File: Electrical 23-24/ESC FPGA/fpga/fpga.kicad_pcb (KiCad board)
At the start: 2 copper layers, 85 x 56 mm, 174 parts, among them J1 SBH11-PBPC-D07-ST-BK, J2 LSHM-110-04.0-L-DV-A-N-K-TR, J3 USB_B_Micro, J4 LSHM-110-04.0-L-DV-A-N-K-TR, J5 Conn_02x06_Top_Bottom, J6 Conn_02x06_Top_Bottom, J7 Conn_02x20_Odd_Even, J8 Conn_02x06_Top_Bottom, J9 Conn_01x01_Pin, SW1 SW_SPDT, SW10 SW_SPDT, SW11 SW_SPDT, SW2 SW_Push, SW3 SW_SPDT, SW4 SW_SPDT, SW5 SW_SPDT, SW6 SW_Push, SW7 SW_Push, SW8 SW_Push, SW9 SW_SPDT, U1 XC6SLX9-TQG144, U12 MIC28515T-E/PHA, U13 FXMA108BQX, U14 FXMA108BQX, U15 FXMA108BQX, U5 MT25QL128ABA1ESE, U6 MIC28515T-E/PHA, U7 MIC28515T-E/PHA, U8 LM74700QDBVRQ1, U9 LM74700QDBVRQ1, X1 KC5032Z100.000C1JX00

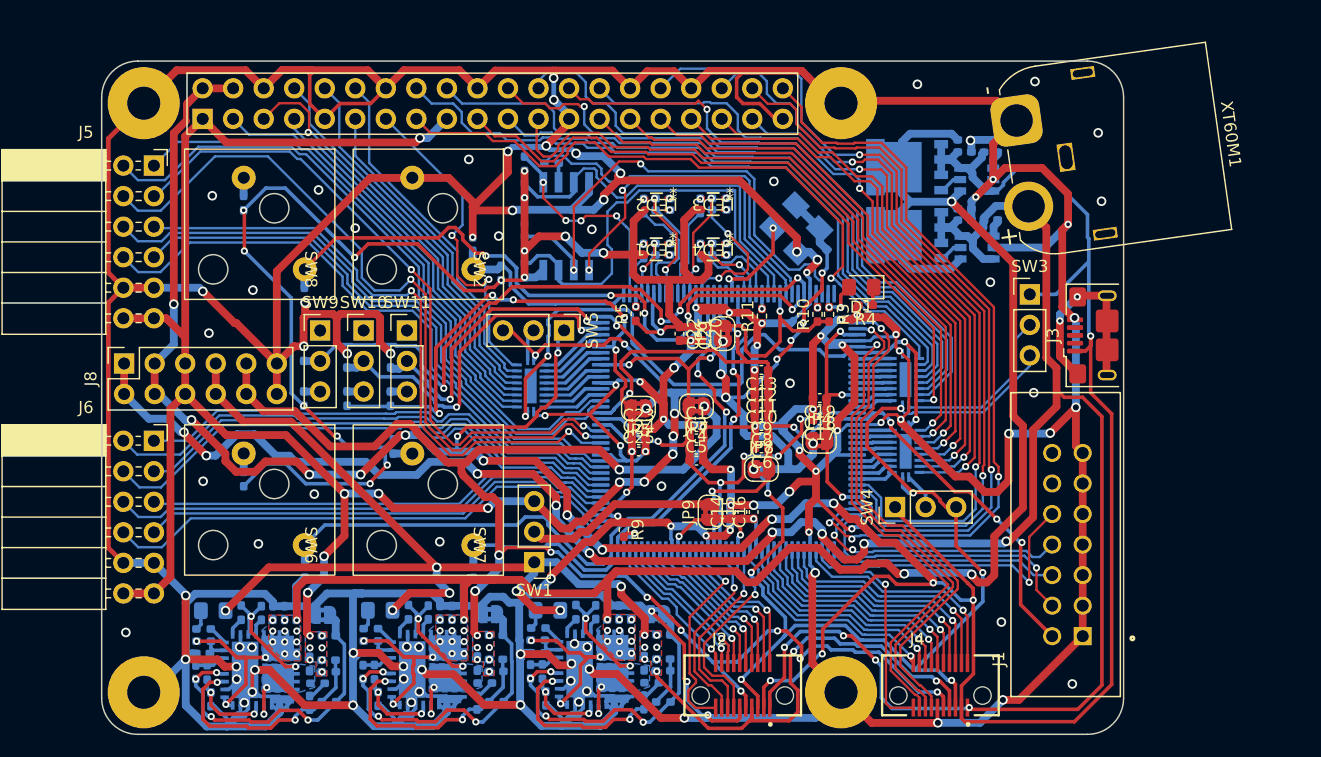
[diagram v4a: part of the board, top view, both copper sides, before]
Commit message: Add silkscreen to FPGA
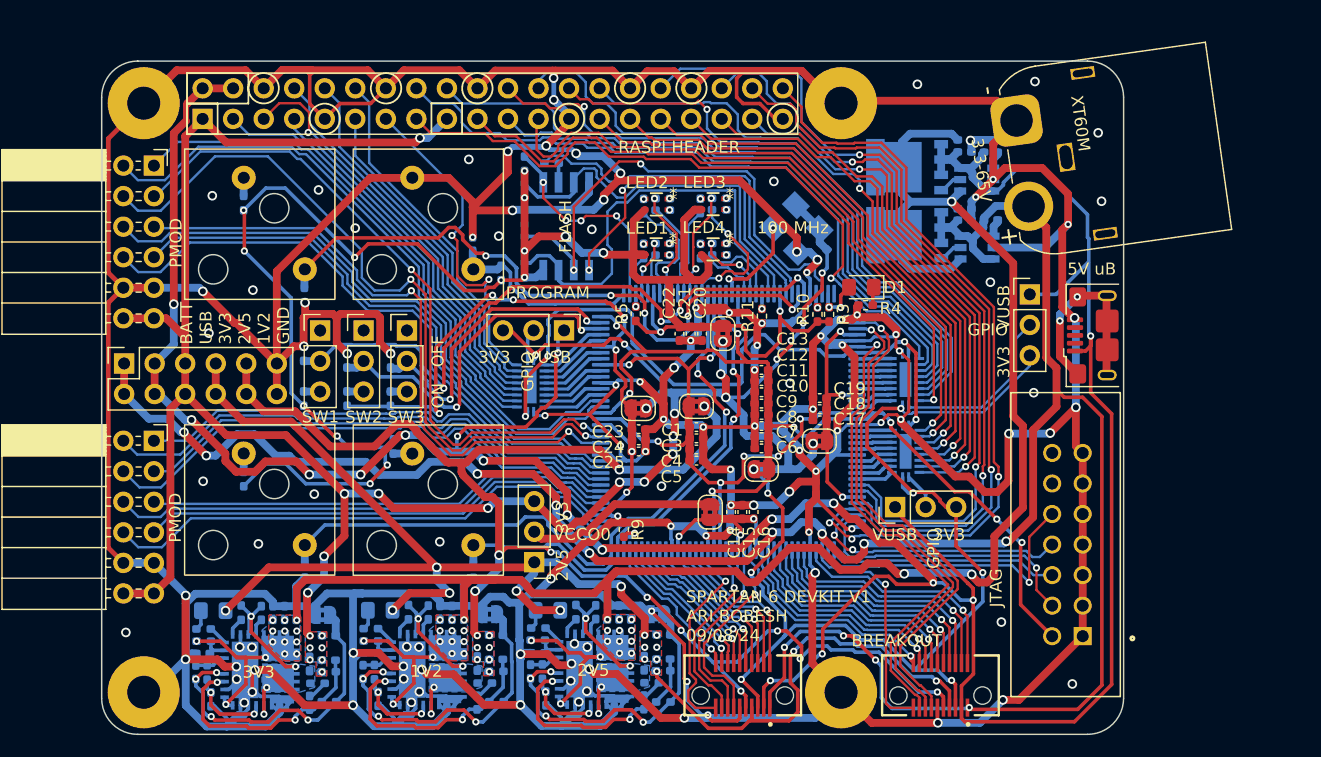
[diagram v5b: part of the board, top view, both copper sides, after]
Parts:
- renumbered XT60M1 to XT60M
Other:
- board text added: "100 MHz"
- board text added: "1V2"
- board text added: "2V5"
- board text added: "2V5 3V3"
- board text added: "3.3-65V"
- board text added: "3V3"
- board text added: "3V3 VUSB"
- board text added: "5V uB"
- board text added: "BATT USB 3V3 2V5 1V2 GND"
- board text added: "BREAKOUT"
- board text added: "BUTTON 1"
- board text added: "BUTTON 2"
- board text added: "BUTTON 3"
- board text added: "FLASH"
- board text added: "GND"
- board text added: "GPIO"
- board text added: "JTAG"
- board text added: "ON OFF"
- board text added: "PMOD"
- board text added: "PROGRAM"
- board text added: "RASPI HEADER"
- board text added: "SPARTAN 6"
- board text added: "SPARTAN 6 DEVKIT V1 ARI BOBESH 09/08/24"
- board text added: "SW1"
- board text added: "SW2"
- board text added: "SW3"
- board text added: "TCK"
- board text added: "TDI"
- board text added: "TDO"
- board text added: "TMS"
- board text added: "VCCO0"
- board text added: "VREF"
- board text added: "VUSB 3V3"
